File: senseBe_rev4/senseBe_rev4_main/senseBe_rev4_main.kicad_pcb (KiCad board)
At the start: 2 copper layers, 56.5 x 40 mm, 64 parts, among them J1 PJ-611-5A_AudioJack, J2 Conn_02x03_Odd_Even, Q1 SI2302, Q2 IRLML6401, Q4 SI2302, Q5 SI2302, Q6 SI2302, Q7 SI2302, SW1 SW_Push_SPDT, SW2 SW_SPST, U1 MDBT42Q, U2 TSSP4056, U3 AP3405, U4 PCF8563T, Y1 Crystal, Y2 Q13FC1350000400

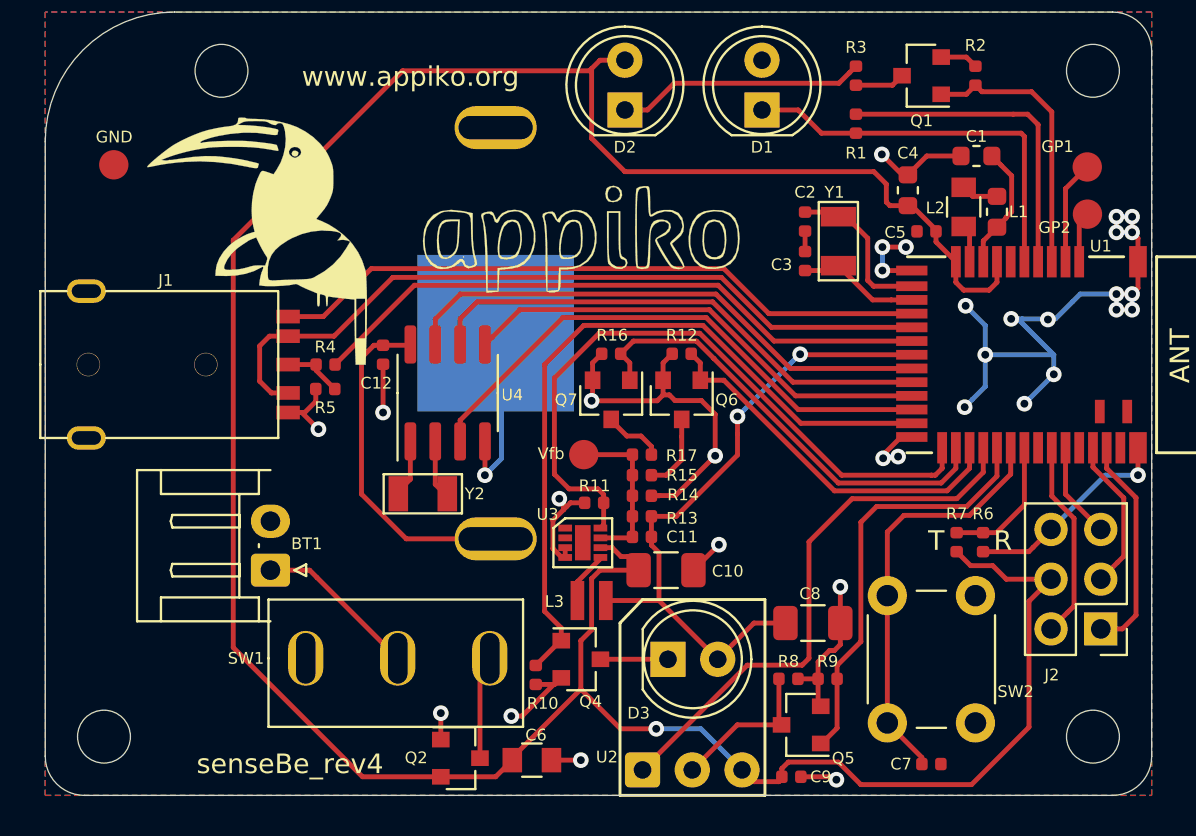
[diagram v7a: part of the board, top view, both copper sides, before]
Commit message: senseBe_rev4 and sense_rev5 gerber files updated.
senseBe_rev4 and sense_rev5 Slider switch footprint updated, sense_rev5 LDR resister position changed.
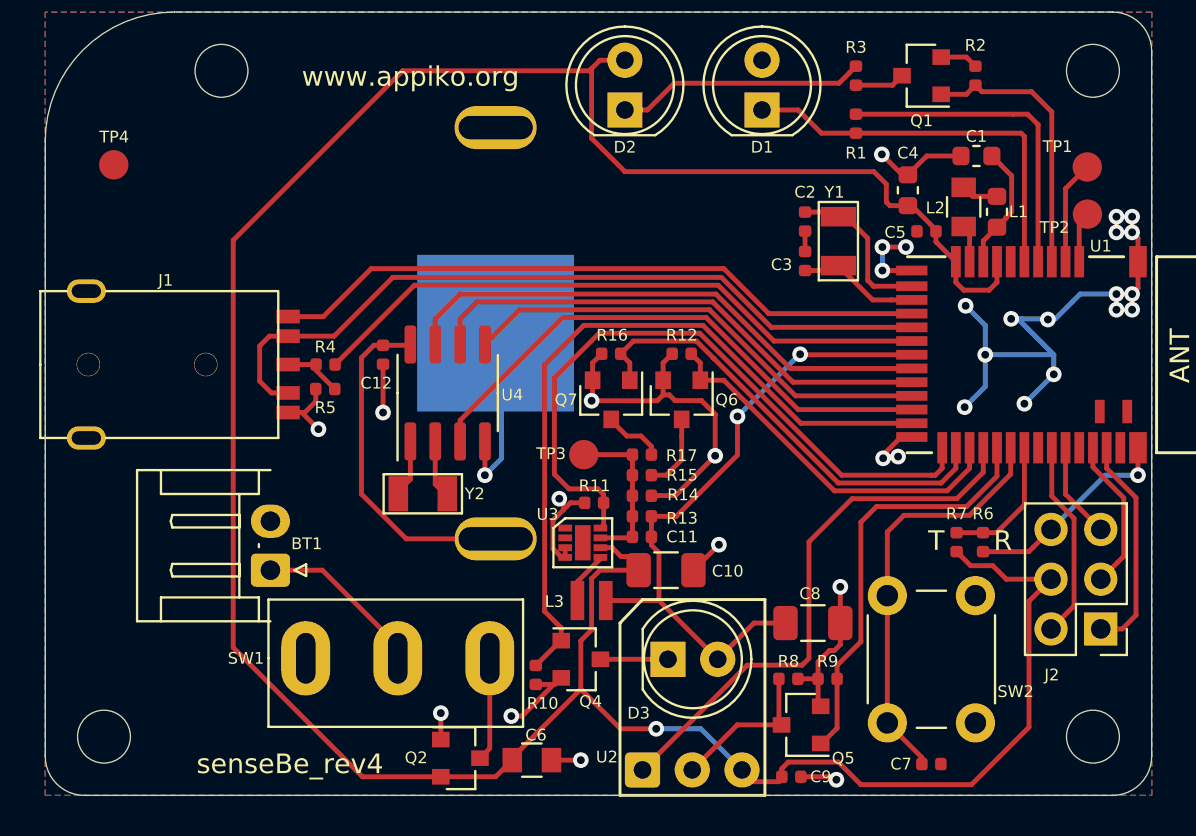
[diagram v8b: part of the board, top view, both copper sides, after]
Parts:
- removed G***: LOGO, sense_fp:OSHW1
- removed G***: Appiko_Logo_2, sense_fp:Appiko_Logo_2
- removed G***: Appiko_LOGO_img, sense_fp:Appiko_LOGO_img
- SW1: footprint sense_fp:SlideSwitch_1P2T_Straight -> sense:SlideSwitch_1P2T_Straight
- renumbered GP1 to TP1, GP2 to TP2, Vfb to TP3, GND to TP4
